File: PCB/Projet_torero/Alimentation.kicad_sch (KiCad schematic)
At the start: 16 parts, among them IC1 MP1475SGJ-P, J2 Conn_01x02, SW3 SW_DPDT_x2, U2 BU33SD5WG-TR

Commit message: modif alim fin ?
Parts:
- removed C12, C13: 0.1µF, symbol Device:C_Small
- removed C15: 47µF, symbol Device:C_Small
- removed IC1: MP1475SGJ-P, SOT65P280X100-8N, symbol MP1475SGJ-P:MP1475SGJ-P
- removed L1: 4.7µF, symbol Device:L_Small
- removed R10, R9: 100k, symbol Device:R_Small
- removed R5: 40.2k, symbol Device:R_Small
- removed R6: 13k, symbol Device:R_Small
- removed R7: 20, symbol Device:R_Small
- removed R8: 16k, symbol Device:R_Small
- added C501, C503: 0.1u, symbol Device:C_Small
- added C502: 47u, symbol Device:C_Small
- added C506: 22u, symbol Device:C_Small
- added IC501: MP1475SGJ-P, SOT65P280X100-8N, symbol MP1475SGJ-P:MP1475SGJ-P
- added L501: 4.7u, symbol Device:L_Small
- added R501, R502: 100k, symbol Device:R_Small
- added R503: 16k, symbol Device:R_Small
- added R504: 7k68, symbol Device:R_Small
- added R505: 40.2k, symbol Device:R_Small
- added R506: 20, symbol Device:R_Small
- C14, C16: value 1µF -> 1u
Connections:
- net +5V: now also C502.1, L501.2, R505.1
- net 7.2V: now also C506.1, IC501.2 (IN), R502.1
- net GND: now also C501.2, C502.2, C506.2, IC501.4 (GND), R504.2
- new net: R503.1, R504.1, R505.2
- new net: C501.1, IC501.7 (VCC), R501.1
- new net: C503.1, R506.1
- new net: C503.2, IC501.3 (SW), L501.1
- new net: IC501.1 (PG), R501.2
- new net: IC501.5 (BST), R506.2
- new net: IC501.6 (EN/SYNC), R502.2
- new net: IC501.8 (FB), R503.2
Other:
- note added: "Connecteur Batterie"
- moved on the sheet: C14, C16

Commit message: modif valeur composants passifs
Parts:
- C501, C503: value 0.1u -> 100n
- L501: value 4.7u -> 4u7
- R505: value 40.2k -> 40k2
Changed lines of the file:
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@@
 			)
 		)
-		(property "Value" "40.2k"
+		(property "Value" "40k2"
 			(at 119.38 148.59 0)
 			(effects
@@
 			)
 		)
-		(property "Value" "0.1u"
+		(property "Value" "100n"
 			(at 55.626 148.844 90)
 			(effects
@@
 			)
 		)
-		(property "Value" "0.1u"
+		(property "Value" "100n"
 			(at 105.41 137.1662 0)
 			(effects
@@
 			)
 		)
-		(property "Value" "4.7u"
+		(property "Value" "4u7"
 			(at 108.204 141.732 90)
 			(effects

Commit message: review sch
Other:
- moved on the sheet: C14, C16, U2
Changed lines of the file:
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@@
 	(paper "A4")
 	(junction
-		(at 171.45 116.84)
+		(at 205.74 120.65)
 		(diameter 0)
 		(color 0 0 0 0)
@@
 	)
 	(junction
-		(at 168.91 116.84)
+		(at 203.2 120.65)
 		(diameter 0)
 		(color 0 0 0 0)
 	)
 	(junction
-		(at 220.98 116.84)
+		(at 255.27 120.65)
 		(diameter 0)
 		(color 0 0 0 0)
@@
 	)
 	(junction
-		(at 193.04 135.89)
+		(at 227.33 139.7)
 		(diameter 0)
 		(color 0 0 0 0)
@@
 	(wire
 		(pts
-			(xy 168.91 116.84) (xy 168.91 123.19)
+			(xy 203.2 120.65) (xy 203.2 127)
 		)
 		(stroke
@@
 	(wire
 		(pts
-			(xy 168.91 135.89) (xy 193.04 135.89)
+			(xy 203.2 139.7) (xy 227.33 139.7)
 		)
 		(stroke
@@
 	(wire
 		(pts
-			(xy 168.91 128.27) (xy 168.91 135.89)
+			(xy 203.2 132.08) (xy 203.2 139.7)
 		)
 		(stroke
@@
 	(wire
 		(pts
-			(xy 220.98 116.84) (xy 224.79 116.84)
+			(xy 255.27 120.65) (xy 259.08 120.65)
 		)
 		(stroke
@@
 	(wire
 		(pts
-			(xy 213.36 116.84) (xy 220.98 116.84)
+			(xy 247.65 120.65) (xy 255.27 120.65)
 		)
 		(stroke
@@
 	(wire
 		(pts
-			(xy 168.91 116.84) (xy 171.45 116.84)
+			(xy 203.2 120.65) (xy 205.74 120.65)
 		)
 		(stroke
@@
 	(wire
 		(pts
-			(xy 193.04 134.62) (xy 193.04 135.89)
+			(xy 227.33 138.43) (xy 227.33 139.7)
 		)
 		(stroke
@@
 	(wire
 		(pts
-			(xy 171.45 116.84) (xy 171.45 119.38)
+			(xy 205.74 120.65) (xy 205.74 123.19)
 		)
 		(stroke
@@
 	(wire
 		(pts
-			(xy 161.29 116.84) (xy 168.91 116.84)
+			(xy 195.58 120.65) (xy 203.2 120.65)
 		)
 		(stroke
@@
 	(wire
 		(pts
-			(xy 171.45 119.38) (xy 172.72 119.38)
+			(xy 205.74 123.19) (xy 207.01 123.19)
 		)
 		(stroke
@@
 	(wire
 		(pts
-			(xy 171.45 116.84) (xy 172.72 116.84)
+			(xy 205.74 120.65) (xy 207.01 120.65)
 		)
 		(stroke
@@
 	(symbol
 		(lib_id "power:+3.3V")
-		(at 224.79 116.84 270)
+		(at 259.08 120.65 270)
 		(unit 1)
 		(exclude_from_sim no)
@@
 		(fields_autoplaced yes)
 		(property "Reference" "#PWR028"
-			(at 220.98 116.84 0)
+			(at 255.27 120.65 0)
 			(effects
 				(font
@@
 		)
 		(property "Value" "+3.3V"
-			(at 228.6 116.8399 90)
+			(at 262.89 120.6499 90)
 			(effects
 				(font
@@
 		)
 		(property "Footprint" ""
-			(at 224.79 116.84 0)
+			(at 259.08 120.65 0)
 			(effects
 				(font
@@
 		)
 		(property "Datasheet" ""
-			(at 224.79 116.84 0)
+			(at 259.08 120.65 0)
 			(effects
 				(font
@@
 		)
 		(property "Description" "Power symbol creates a global label with name \"+3.3V\""
-			(at 224.79 116.84 0)
+			(at 259.08 120.65 0)
 			(effects
 				(font
@@
 	(symbol
 		(lib_id "power:GND")
-		(at 220.98 121.92 0)
+		(at 255.27 125.73 0)
 		(unit 1)
 		(exclude_from_sim no)
@@
 		(fields_autoplaced yes)
 		(property "Reference" "#PWR025"
-			(at 220.98 128.27 0)
+			(at 255.27 132.08 0)
 			(effects
 				(font
@@
 		)
 		(property "Value" "GND"
-			(at 220.98 127 0)
+			(at 255.27 130.81 0)
 			(effects
 				(font
@@
 		)
 		(property "Footprint" ""
-			(at 220.98 121.92 0)
+			(at 255.27 125.73 0)
 			(effects
 				(font
@@
 		)
 		(property "Datasheet" ""
-			(at 220.98 121.92 0)
+			(at 255.27 125.73 0)
 			(effects
 				(font
@@
 		)
 		(property "Description" "Power symbol creates a global label with name \"GND\" , ground"
-			(at 220.98 121.92 0)
+			(at 255.27 125.73 0)
 			(effects
 				(font
@@
 	(symbol
 		(lib_id "2024-10-01_06-18-21:BU33SD5WG-TR")
-		(at 172.72 116.84 0)
+		(at 207.01 120.65 0)
 		(unit 1)
 		(exclude_from_sim no)
@@
 		(fields_autoplaced yes)
 		(property "Reference" "U2"
-			(at 193.04 106.68 0)
+			(at 227.33 110.49 0)
 			(effects
 				(font
@@
 		)
 		(property "Value" "BU33SD5WG-TR"
-			(at 193.04 109.22 0)
+			(at 227.33 113.03 0)
 			(effects
 				(font
@@
 		)
 		(property "Footprint" "SSOP5_ROM"
-			(at 172.72 116.84 0)
+			(at 207.01 120.65 0)
 			(effects
 				(font
@@
 		)
 		(property "Datasheet" "BU33SD5WG-TR"
-			(at 172.72 116.84 0)
+			(at 207.01 120.65 0)
 			(effects
 				(font
@@
 		)
 		(property "Description" ""
-			(at 172.72 116.84 0)
+			(at 207.01 120.65 0)
 			(effects
 				(font
@@
 	(symbol
 		(lib_id "Device:C_Small")
-		(at 168.91 125.73 0)
+		(at 203.2 129.54 0)
 		(unit 1)
 		(exclude_from_sim no)
@@
 		(dnp no)
 		(property "Reference" "C14"
-			(at 164.846 125.984 90)
+			(at 199.136 129.794 90)
 			(effects
 				(font
@@
 		)
 		(property "Value" "1u"
-			(at 162.306 125.984 90)
+			(at 196.596 129.794 90)
 			(effects
 				(font
@@
 		)
 		(property "Footprint" ""
-			(at 168.91 125.73 0)
+			(at 203.2 129.54 0)
 			(effects
 				(font
@@
 		)
 		(property "Datasheet" "~"
-			(at 168.91 125.73 0)
+			(at 203.2 129.54 0)
 			(effects
 				(font
@@
 		)
 		(property "Description" "Unpolarized capacitor, small symbol"
-			(at 168.91 125.73 0)
+			(at 203.2 129.54 0)
 			(effects
 				(font
@@
 	(symbol
 		(lib_id "Device:C_Small")
-		(at 220.98 119.38 180)
+		(at 255.27 123.19 180)
 		(unit 1)
 		(exclude_from_sim no)
@@
 		(dnp no)
 		(property "Reference" "C16"
-			(at 225.044 119.126 90)
+			(at 259.334 122.936 90)
 			(effects
 				(font
@@
 		)
 		(property "Value" "1u"
-			(at 227.584 119.126 90)
+			(at 261.874 122.936 90)
 			(effects
 				(font
@@
 		)
 		(property "Footprint" ""
-			(at 220.98 119.38 0)
+			(at 255.27 123.19 0)
 			(effects
 				(font
@@
 		)
 		(property "Datasheet" "~"
-			(at 220.98 119.38 0)
+			(at 255.27 123.19 0)
 			(effects
 				(font
@@
 		)
 		(property "Description" "Unpolarized capacitor, small symbol"
-			(at 220.98 119.38 0)
+			(at 255.27 123.19 0)
 			(effects
 				(font
@@
 	(symbol
 		(lib_id "power:GND")
-		(at 193.04 135.89 0)
+		(at 227.33 139.7 0)
 		(unit 1)
 		(exclude_from_sim no)
@@
 		(fields_autoplaced yes)
 		(property "Reference" "#PWR022"
-			(at 193.04 142.24 0)
+			(at 227.33 146.05 0)
 			(effects
 				(font
@@
 		)
 		(property "Value" "GND"
-			(at 193.04 140.97 0)
+			(at 227.33 144.78 0)
 			(effects
 				(font
@@
 		)
 		(property "Footprint" ""
-			(at 193.04 135.89 0)
+			(at 227.33 139.7 0)
 			(effects
 				(font
@@
 		)
 		(property "Datasheet" ""
-			(at 193.04 135.89 0)
+			(at 227.33 139.7 0)
 			(effects
 				(font
@@
 		)
 		(property "Description" "Power symbol creates a global label with name \"GND\" , ground"
-			(at 193.04 135.89 0)
+			(at 227.33 139.7 0)
 			(effects
 				(font
@@
 	(symbol
 		(lib_id "power:+5V")
-		(at 161.29 116.84 90)
+		(at 195.58 120.65 90)
 		(unit 1)
 		(exclude_from_sim no)
@@
 		(dnp no)
 		(property "Reference" "#PWR026"
-			(at 165.1 116.84 0)
+			(at 199.39 120.65 0)
 			(effects
 				(font
@@
 		)
 		(property "Value" "+5V"
-			(at 158.242 116.84 90)
+			(at 192.532 120.65 90)
 			(effects
 				(font
@@
 		)
 		(property "Footprint" ""
-			(at 161.29 116.84 0)
+			(at 195.58 120.65 0)
 			(effects
 				(font
@@
 		)
 		(property "Datasheet" ""
-			(at 161.29 116.84 0)
+			(at 195.58 120.65 0)
 			(effects
 				(font
@@
 		)
 		(property "Description" "Power symbol creates a global label with name \"+5V\""
-			(at 161.29 116.84 0)
-			(effects
-				(font
+			(at 195.58 120.65 0)
+			(effects
+				(font

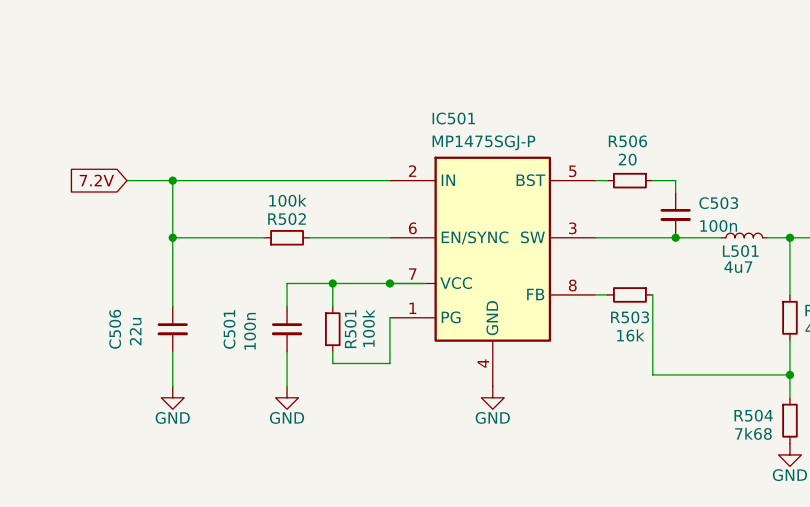
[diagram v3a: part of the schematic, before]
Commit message: review sch après vérif prof
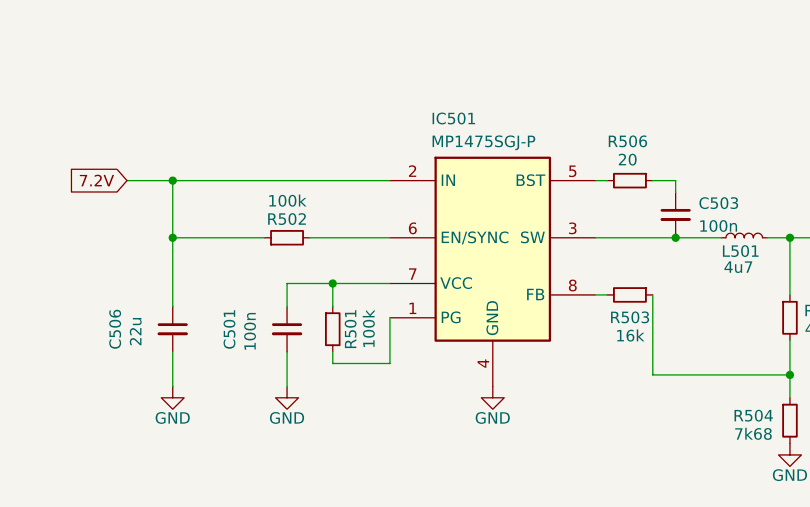
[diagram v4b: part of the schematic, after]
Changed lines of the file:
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@@
-	)
-	(junction
-		(at 71.12 143.51)
-		(diameter 0)
-		(color 0 0 0 0)
 	)
 	(junction
@@
 		)
 		(stroke
-			(width 0)
-			(type default)
-		)
-	)
-	(wire
-		(pts
-			(xy 74.93 143.51) (xy 71.12 143.51)
-		)
-		(stroke

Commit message: changement schéma
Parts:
- renumbered C506 to C501, C501 to C502, C502 to C504, C14 to C505, C16 to C506, J2 to J501, R502 to R501, R501 to R502, R506 to R503, R503 to R504, R504 to R506, SW3 to SW501, U2 to U501
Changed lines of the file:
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@@
 		(on_board yes)
 		(dnp no)
-		(property "Reference" "#PWR0504"
+		(property "Reference" "#PWR0505"
 			(at 115.57 167.64 0)
 			(effects
@@
 			(project "Projet_torero"
 				(path "/04e1eb47-a2c4-462b-bef7-377d9515a2c0/b3b2826c-2e3c-42fe-bcd6-22fcd6249c25"
-					(reference "#PWR0504")
+					(reference "#PWR0505")
 					(unit 1)
 				)
@@
 		(on_board yes)
 		(dnp no)
-		(property "Reference" "#PWR0503"
+		(property "Reference" "#PWR0504"
 			(at 82.55 161.29 0)
 			(effects
@@
 			(project "Projet_torero"
 				(path "/04e1eb47-a2c4-462b-bef7-377d9515a2c0/b3b2826c-2e3c-42fe-bcd6-22fcd6249c25"
-					(reference "#PWR0503")
+					(reference "#PWR0504")
 					(unit 1)
 				)
@@
 		(on_board yes)
 		(dnp no)
-		(property "Reference" "C501"
+		(property "Reference" "C502"
 			(at 53.34 148.59 90)
 			(effects
@@
 			(project "Projet_torero"
 				(path "/04e1eb47-a2c4-462b-bef7-377d9515a2c0/b3b2826c-2e3c-42fe-bcd6-22fcd6249c25"
-					(reference "C501")
+					(reference "C502")
 					(unit 1)
 				)
@@
 		(dnp no)
 		(fields_autoplaced yes)
-		(property "Reference" "#PWR028"
+		(property "Reference" "#PWR0511"
 			(at 255.27 120.65 0)
 			(effects
@@
 			(project ""
 				(path "/04e1eb47-a2c4-462b-bef7-377d9515a2c0/b3b2826c-2e3c-42fe-bcd6-22fcd6249c25"
-					(reference "#PWR028")
+					(reference "#PWR0511")
 					(unit 1)
 				)
@@
 		(on_board yes)
 		(dnp no)
-		(property "Reference" "C506"
+		(property "Reference" "C501"
 			(at 40.64 148.59 90)
 			(effects
@@
 			(project "Projet_torero"
 				(path "/04e1eb47-a2c4-462b-bef7-377d9515a2c0/b3b2826c-2e3c-42fe-bcd6-22fcd6249c25"
-					(reference "C506")
+					(reference "C501")
 					(unit 1)
 				)
@@
 		(dnp no)
 		(fields_autoplaced yes)
-		(property "Reference" "SW3"
+		(property "Reference" "SW501"
 			(at 62.23 29.21 0)
 			(effects
@@
 			(project ""
 				(path "/04e1eb47-a2c4-462b-bef7-377d9515a2c0/b3b2826c-2e3c-42fe-bcd6-22fcd6249c25"
-					(reference "SW3")
+					(reference "SW501")
 					(unit 1)
 				)
@@
 		(dnp no)
 		(fields_autoplaced yes)
-		(property "Reference" "#PWR025"
+		(property "Reference" "#PWR0510"
 			(at 255.27 132.08 0)
 			(effects
@@
 			(project "Projet_torero"
 				(path "/04e1eb47-a2c4-462b-bef7-377d9515a2c0/b3b2826c-2e3c-42fe-bcd6-22fcd6249c25"
-					(reference "#PWR025")
+					(reference "#PWR0510")
 					(unit 1)
 				)
@@
 		(dnp no)
 		(fields_autoplaced yes)
-		(property "Reference" "U2"
+		(property "Reference" "U501"
 			(at 227.33 110.49 0)
 			(effects
@@
 			(project ""
 				(path "/04e1eb47-a2c4-462b-bef7-377d9515a2c0/b3b2826c-2e3c-42fe-bcd6-22fcd6249c25"
-					(reference "U2")
+					(reference "U501")
 					(unit 1)
 				)
@@
 		(on_board yes)
 		(dnp no)
-		(property "Reference" "#PWR0505"
+		(property "Reference" "#PWR0507"
 			(at 127 167.64 0)
 			(effects
@@
 			(project "Projet_torero"
 				(path "/04e1eb47-a2c4-462b-bef7-377d9515a2c0/b3b2826c-2e3c-42fe-bcd6-22fcd6249c25"
-					(reference "#PWR0505")
+					(reference "#PWR0507")
 					(unit 1)
 				)
@@
 		(on_board yes)
 		(dnp no)
-		(property "Reference" "R501"
+		(property "Reference" "R502"
 			(at 66.802 148.59 90)
 			(effects
@@
 			(project "Projet_torero"
 				(path "/04e1eb47-a2c4-462b-bef7-377d9515a2c0/b3b2826c-2e3c-42fe-bcd6-22fcd6249c25"
-					(reference "R501")
+					(reference "R502")
 					(unit 1)
 				)
@@
 		(on_board yes)
 		(dnp no)
-		(property "Reference" "C14"
+		(property "Reference" "C505"
 			(at 199.136 129.794 90)
 			(effects
@@
 			(project "Projet_torero"
 				(path "/04e1eb47-a2c4-462b-bef7-377d9515a2c0/b3b2826c-2e3c-42fe-bcd6-22fcd6249c25"
-					(reference "C14")
+					(reference "C505")
 					(unit 1)
 				)
@@
 		(dnp no)
 		(fields_autoplaced yes)
-		(property "Reference" "#PWR021"
+		(property "Reference" "#PWR0503"
 			(at 63.5 52.07 0)
 			(effects
@@
 			(project ""
 				(path "/04e1eb47-a2c4-462b-bef7-377d9515a2c0/b3b2826c-2e3c-42fe-bcd6-22fcd6249c25"
-					(reference "#PWR021")
+					(reference "#PWR0503")
 					(unit 1)
 				)
@@
 		(dnp no)
 		(fields_autoplaced yes)
-		(property "Reference" "J2"
+		(property "Reference" "J501"
 			(at 35.56 31.75 0)
 			(effects
@@
 			(project ""
 				(path "/04e1eb47-a2c4-462b-bef7-377d9515a2c0/b3b2826c-2e3c-42fe-bcd6-22fcd6249c25"
-					(reference "J2")
+					(reference "J501")
 					(unit 1)
 				)
@@
 		(on_board yes)
 		(dnp no)
-		(property "Reference" "R502"
+		(property "Reference" "R501"
 			(at 59.69 136.398 90)
 			(effects
@@
 			(project "Projet_torero"
 				(path "/04e1eb47-a2c4-462b-bef7-377d9515a2c0/b3b2826c-2e3c-42fe-bcd6-22fcd6249c25"
-					(reference "R502")
+					(reference "R501")
 					(unit 1)
 				)
@@
 		(on_board yes)
 		(dnp no)
-		(property "Reference" "R506"
+		(property "Reference" "R503"
 			(at 97.536 127.762 90)
 			(effects
@@
 			(project "Projet_torero"
 				(path "/04e1eb47-a2c4-462b-bef7-377d9515a2c0/b3b2826c-2e3c-42fe-bcd6-22fcd6249c25"
-					(reference "R506")
+					(reference "R503")
 					(unit 1)
 				)
@@
 		(on_board yes)
 		(dnp no)
-		(property "Reference" "R504"
+		(property "Reference" "R506"
 			(at 111.506 158.242 0)
 			(effects
@@
 			(project "Projet_torero"
 				(path "/04e1eb47-a2c4-462b-bef7-377d9515a2c0/b3b2826c-2e3c-42fe-bcd6-22fcd6249c25"
-					(reference "R504")
+					(reference "R506")
 					(unit 1)
 				)
@@
 		(on_board yes)
 		(dnp no)
-		(property "Reference" "R503"
+		(property "Reference" "R504"
 			(at 97.79 147.32 90)
 			(effects
@@
 			(project "Projet_torero"
 				(path "/04e1eb47-a2c4-462b-bef7-377d9515a2c0/b3b2826c-2e3c-42fe-bcd6-22fcd6249c25"
-					(reference "R503")
+					(reference "R504")
 					(unit 1)
 				)
@@
 		(on_board yes)
 		(dnp no)
-		(property "Reference" "#PWR0509"
+		(property "Reference" "#PWR0501"
 			(at 46.99 161.29 0)
 			(effects
@@
 			(project "Projet_torero"
 				(path "/04e1eb47-a2c4-462b-bef7-377d9515a2c0/b3b2826c-2e3c-42fe-bcd6-22fcd6249c25"
-					(reference "#PWR0509")
+					(reference "#PWR0501")
 					(unit 1)
 				)
@@
 		(on_board yes)
 		(dnp no)
-		(property "Reference" "C16"
+		(property "Reference" "C506"
 			(at 259.334 122.936 90)
 			(effects
@@
 			(project "Projet_torero"
 				(path "/04e1eb47-a2c4-462b-bef7-377d9515a2c0/b3b2826c-2e3c-42fe-bcd6-22fcd6249c25"
-					(reference "C16")
+					(reference "C506")
 					(unit 1)
 				)
@@
 		(on_board yes)
 		(dnp no)
-		(property "Reference" "C502"
+		(property "Reference" "C504"
 			(at 131.064 153.924 90)
 			(effects
@@
 			(project "Projet_torero"
 				(path "/04e1eb47-a2c4-462b-bef7-377d9515a2c0/b3b2826c-2e3c-42fe-bcd6-22fcd6249c25"
-					(reference "C502")
+					(reference "C504")
 					(unit 1)
 				)
@@
 		(dnp no)
 		(fields_autoplaced yes)
-		(property "Reference" "#PWR022"
+		(property "Reference" "#PWR0509"
 			(at 227.33 146.05 0)
 			(effects
@@
 			(project ""
 				(path "/04e1eb47-a2c4-462b-bef7-377d9515a2c0/b3b2826c-2e3c-42fe-bcd6-22fcd6249c25"
-					(reference "#PWR022")
+					(reference "#PWR0509")
 					(unit 1)
 				)
@@
 		(on_board yes)
 		(dnp no)
-		(property "Reference" "#PWR026"
+		(property "Reference" "#PWR0508"
 			(at 199.39 120.65 0)
 			(effects
@@
 			(project "Projet_torero"
 				(path "/04e1eb47-a2c4-462b-bef7-377d9515a2c0/b3b2826c-2e3c-42fe-bcd6-22fcd6249c25"
-					(reference "#PWR026")
-					(unit 1)
-				)
+					(reference "#PWR0508")
+					(unit 1)
+				)

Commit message: modif placement composant
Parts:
- C501: footprint (none) -> Capacitor_SMD:C_0805_2012Metric_Pad1.18x1.45mm_HandSolder
- C502, C503: footprint (none) -> Capacitor_SMD:C_0402_1005Metric
- C504: footprint (none) -> Capacitor_SMD:C_0603_1608Metric_Pad1.08x0.95mm_HandSolder
- C505, C506: footprint (none) -> Capacitor_SMD:C_0603_1608Metric
- J501: footprint (none) -> Connector_JST:JST_XH_S2B-XH-A_1x02_P2.50mm_Horizontal
- L501: footprint (none) -> Inductor_SMD:L_0603_1608Metric_Pad1.05x0.95mm_HandSolder
- R501, R502, R503, R504, R505, R506: footprint (none) -> Resistor_SMD:R_0603_1608Metric
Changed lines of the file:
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@@
 			)
 		)
-		(property "Footprint" ""
+		(property "Footprint" "Resistor_SMD:R_0603_1608Metric"
 			(at 115.57 147.32 0)
 			(effects
@@
 			)
 		)
-		(property "Footprint" ""
+		(property "Footprint" "Capacitor_SMD:C_0402_1005Metric"
 			(at 59.69 148.59 0)
 			(effects
@@
 			)
 		)
-		(property "Footprint" ""
+		(property "Footprint" "Capacitor_SMD:C_0805_2012Metric_Pad1.18x1.45mm_HandSolder"
 			(at 46.99 148.59 0)
 			(effects
@@
 			)
 		)
-		(property "Footprint" ""
+		(property "Footprint" "Capacitor_SMD:C_0402_1005Metric"
 			(at 102.87 135.89 0)
 			(effects
@@
 			)
 		)
-		(property "Footprint" ""
+		(property "Footprint" "Inductor_SMD:L_0603_1608Metric_Pad1.05x0.95mm_HandSolder"
 			(at 110.49 138.43 0)
 			(effects
@@
 			)
 		)
-		(property "Footprint" ""
+		(property "Footprint" "Resistor_SMD:R_0603_1608Metric"
 			(at 64.77 148.59 0)
 			(effects
@@
 			)
 		)
-		(property "Footprint" ""
+		(property "Footprint" "Capacitor_SMD:C_0603_1608Metric"
 			(at 203.2 129.54 0)
 			(effects
@@
 			)
 		)
-		(property "Footprint" ""
+		(property "Footprint" "Connector_JST:JST_XH_S2B-XH-A_1x02_P2.50mm_Horizontal"
 			(at 35.56 40.64 0)
 			(effects
@@
 			)
 		)
-		(property "Footprint" ""
+		(property "Footprint" "Resistor_SMD:R_0603_1608Metric"
 			(at 59.69 138.43 0)
 			(effects
@@
 			)
 		)
-		(property "Footprint" ""
+		(property "Footprint" "Resistor_SMD:R_0603_1608Metric"
 			(at 97.79 132.08 0)
 			(effects
@@
 			)
 		)
-		(property "Footprint" ""
+		(property "Footprint" "Resistor_SMD:R_0603_1608Metric"
 			(at 115.57 158.75 0)
 			(effects
@@
 			)
 		)
-		(property "Footprint" ""
+		(property "Footprint" "Resistor_SMD:R_0603_1608Metric"
 			(at 97.79 144.78 0)
 			(effects
@@
 			)
 		)
-		(property "Footprint" ""
+		(property "Footprint" "Capacitor_SMD:C_0603_1608Metric"
 			(at 255.27 123.19 0)
 			(effects
@@
 			)
 		)
-		(property "Footprint" ""
+		(property "Footprint" "Capacitor_SMD:C_0603_1608Metric_Pad1.08x0.95mm_HandSolder"
 			(at 127 153.67 0)
 			(effects
